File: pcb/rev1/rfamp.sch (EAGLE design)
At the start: 17 parts, among them IC1 TS520530, IC2 ADL5523, X1 SAW-B3721

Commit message: Minor changes.
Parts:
- MOV1: value MOV -> (none)
- renumbered R1 to MOV1
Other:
- moved on the sheet: C3, C4, C5, IC1, JP1, POWER, R3
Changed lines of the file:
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@@
 <part name="GND3" library="supply1" deviceset="GND" device=""/>
 <part name="X1" library="qyx-misc" deviceset="SAW-B3721" device=""/>
-<part name="R1" library="rcl" deviceset="R-EU_" device="R0603" value="MOV"/>
+<part name="MOV1" library="rcl" deviceset="R-EU_" device="R0603"/>
 <part name="GND4" library="supply1" deviceset="GND" device=""/>
 <part name="GND5" library="supply1" deviceset="GND" device=""/>
@@
 <instance part="RFIN" gate="G1" x="0" y="71.12"/>
 <instance part="GND1" gate="1" x="5.08" y="53.34"/>
-<instance part="GND2" gate="1" x="2.54" y="2.54"/>
+<instance part="GND2" gate="1" x="22.86" y="99.06"/>
 <instance part="RFOUT" gate="G1" x="182.88" y="71.12" rot="MR0"/>
 <instance part="GND3" gate="1" x="177.8" y="53.34"/>
 <instance part="X1" gate="G$1" x="53.34" y="66.04"/>
-<instance part="R1" gate="G$1" x="20.32" y="63.5" rot="R90"/>
+<instance part="MOV1" gate="G$1" x="20.32" y="63.5" rot="R90"/>
 <instance part="GND4" gate="1" x="48.26" y="53.34"/>
 <instance part="GND5" gate="1" x="53.34" y="53.34"/>
@@
 <instance part="GND10" gate="1" x="167.64" y="78.74"/>
 <instance part="+3V1" gate="G$1" x="167.64" y="99.06"/>
-<instance part="+3V2" gate="G$1" x="58.42" y="25.4"/>
-<instance part="IC1" gate="G$1" x="27.94" y="12.7"/>
-<instance part="C3" gate="G$1" x="43.18" y="10.16" rot="R90"/>
-<instance part="C4" gate="G$1" x="58.42" y="12.7"/>
-<instance part="C5" gate="G$1" x="2.54" y="12.7"/>
-<instance part="GND11" gate="1" x="15.24" y="2.54"/>
-<instance part="GND12" gate="1" x="50.8" y="2.54"/>
-<instance part="GND13" gate="1" x="58.42" y="2.54"/>
-<instance part="P+1" gate="1" x="2.54" y="25.4"/>
-<instance part="JP1" gate="G$1" x="-20.32" y="15.24"/>
-<instance part="GND14" gate="1" x="-10.16" y="2.54"/>
+<instance part="+3V2" gate="G$1" x="78.74" y="121.92"/>
+<instance part="IC1" gate="G$1" x="48.26" y="109.22"/>
+<instance part="C3" gate="G$1" x="63.5" y="106.68" rot="R90"/>
+<instance part="C4" gate="G$1" x="78.74" y="109.22"/>
+<instance part="C5" gate="G$1" x="22.86" y="109.22"/>
+<instance part="GND11" gate="1" x="35.56" y="99.06"/>
+<instance part="GND12" gate="1" x="71.12" y="99.06"/>
+<instance part="GND13" gate="1" x="78.74" y="99.06"/>
+<instance part="P+1" gate="1" x="22.86" y="121.92"/>
+<instance part="JP1" gate="G$1" x="0" y="111.76"/>
+<instance part="GND14" gate="1" x="10.16" y="99.06"/>
 <instance part="IC2" gate="G$1" x="127" y="68.58"/>
 <instance part="GND15" gate="1" x="144.78" y="53.34"/>
-<instance part="R3" gate="G$1" x="71.12" y="17.78"/>
-<instance part="POWER" gate="G$1" x="81.28" y="12.7"/>
-<instance part="GND16" gate="1" x="81.28" y="2.54"/>
+<instance part="R3" gate="G$1" x="91.44" y="114.3"/>
+<instance part="POWER" gate="G$1" x="101.6" y="109.22"/>
+<instance part="GND16" gate="1" x="101.6" y="99.06"/>
 </instances>
 <busses>
@@
 <segment>
 <pinref part="GND8" gate="1" pin="GND"/>
-<pinref part="R1" gate="G$1" pin="1"/>
+<pinref part="MOV1" gate="G$1" pin="1"/>
 <wire x1="20.32" y1="55.88" x2="20.32" y2="58.42" width="0.1524" layer="91"/>
 </segment>
@@
 <pinref part="C5" gate="G$1" pin="2"/>
 <pinref part="GND2" gate="1" pin="GND"/>
-<wire x1="2.54" y1="7.62" x2="2.54" y2="5.08" width="0.1524" layer="91"/>
+<wire x1="22.86" y1="104.14" x2="22.86" y2="101.6" width="0.1524" layer="91"/>
 </segment>
 <segment>
 <pinref part="IC1" gate="G$1" pin="GND"/>
 <pinref part="GND11" gate="1" pin="GND"/>
-<wire x1="17.78" y1="7.62" x2="15.24" y2="7.62" width="0.1524" layer="91"/>
-<wire x1="15.24" y1="7.62" x2="15.24" y2="5.08" width="0.1524" layer="91"/>
+<wire x1="38.1" y1="104.14" x2="35.56" y2="104.14" width="0.1524" layer="91"/>
+<wire x1="35.56" y1="104.14" x2="35.56" y2="101.6" width="0.1524" layer="91"/>
 </segment>
 <segment>
 <pinref part="C4" gate="G$1" pin="2"/>
 <pinref part="GND13" gate="1" pin="GND"/>
-<wire x1="58.42" y1="7.62" x2="58.42" y2="5.08" width="0.1524" layer="91"/>
+<wire x1="78.74" y1="104.14" x2="78.74" y2="101.6" width="0.1524" layer="91"/>
 </segment>
 <segment>
 <pinref part="C3" gate="G$1" pin="2"/>
 <pinref part="GND12" gate="1" pin="GND"/>
-<wire x1="48.26" y1="10.16" x2="50.8" y2="10.16" width="0.1524" layer="91"/>
-<wire x1="50.8" y1="10.16" x2="50.8" y2="5.08" width="0.1524" layer="91"/>
+<wire x1="68.58" y1="106.68" x2="71.12" y2="106.68" width="0.1524" layer="91"/>
+<wire x1="71.12" y1="106.68" x2="71.12" y2="101.6" width="0.1524" layer="91"/>
 </segment>
 <segment>
 <pinref part="JP1" gate="G$1" pin="1"/>
 <pinref part="GND14" gate="1" pin="GND"/>
-<wire x1="-12.7" y1="15.24" x2="-10.16" y2="15.24" width="0.1524" layer="91"/>
-<wire x1="-10.16" y1="15.24" x2="-10.16" y2="5.08" width="0.1524" layer="91"/>
+<wire x1="7.62" y1="111.76" x2="10.16" y2="111.76" width="0.1524" layer="91"/>
+<wire x1="10.16" y1="111.76" x2="10.16" y2="101.6" width="0.1524" layer="91"/>
 </segment>
 <segment>
@@
 <pinref part="POWER" gate="G$1" pin="C"/>
 <pinref part="GND16" gate="1" pin="GND"/>
-<wire x1="81.28" y1="7.62" x2="81.28" y2="5.08" width="0.1524" layer="91"/>
+<wire x1="101.6" y1="104.14" x2="101.6" y2="101.6" width="0.1524" layer="91"/>
 </segment>
 </net>
@@
 <segment>
 <pinref part="RFIN" gate="G1" pin="1"/>
-<pinref part="R1" gate="G$1" pin="2"/>
+<pinref part="MOV1" gate="G$1" pin="2"/>
 <wire x1="2.54" y1="71.12" x2="20.32" y2="71.12" width="0.1524" layer="91"/>
 <wire x1="20.32" y1="71.12" x2="20.32" y2="68.58" width="0.1524" layer="91"/>
@@
 <pinref part="IC1" gate="G$1" pin="VOUT"/>
 <pinref part="C4" gate="G$1" pin="1"/>
-<wire x1="38.1" y1="17.78" x2="58.42" y2="17.78" width="0.1524" layer="91"/>
-<wire x1="58.42" y1="17.78" x2="58.42" y2="15.24" width="0.1524" layer="91"/>
+<wire x1="58.42" y1="114.3" x2="78.74" y2="114.3" width="0.1524" layer="91"/>
+<wire x1="78.74" y1="114.3" x2="78.74" y2="111.76" width="0.1524" layer="91"/>
 <pinref part="+3V2" gate="G$1" pin="+3V3"/>
-<wire x1="58.42" y1="17.78" x2="58.42" y2="22.86" width="0.1524" layer="91"/>
-<junction x="58.42" y="17.78"/>
+<wire x1="78.74" y1="114.3" x2="78.74" y2="119.38" width="0.1524" layer="91"/>
+<junction x="78.74" y="114.3"/>
 <pinref part="R3" gate="G$1" pin="1"/>
-<wire x1="58.42" y1="17.78" x2="66.04" y2="17.78" width="0.1524" layer="91"/>
+<wire x1="78.74" y1="114.3" x2="86.36" y2="114.3" width="0.1524" layer="91"/>
 </segment>
 </net>
@@
 <pinref part="C5" gate="G$1" pin="1"/>
 <pinref part="P+1" gate="1" pin="+5V"/>
-<wire x1="2.54" y1="15.24" x2="2.54" y2="17.78" width="0.1524" layer="91"/>
+<wire x1="22.86" y1="111.76" x2="22.86" y2="114.3" width="0.1524" layer="91"/>
 <pinref part="IC1" gate="G$1" pin="VIN"/>
-<wire x1="2.54" y1="17.78" x2="2.54" y2="22.86" width="0.1524" layer="91"/>
-<wire x1="17.78" y1="17.78" x2="15.24" y2="17.78" width="0.1524" layer="91"/>
-<junction x="2.54" y="17.78"/>
+<wire x1="22.86" y1="114.3" x2="22.86" y2="119.38" width="0.1524" layer="91"/>
+<wire x1="38.1" y1="114.3" x2="35.56" y2="114.3" width="0.1524" layer="91"/>
+<junction x="22.86" y="114.3"/>
 <pinref part="IC1" gate="G$1" pin="CE"/>
-<wire x1="15.24" y1="17.78" x2="2.54" y2="17.78" width="0.1524" layer="91"/>
-<wire x1="17.78" y1="12.7" x2="15.24" y2="12.7" width="0.1524" layer="91"/>
-<wire x1="15.24" y1="12.7" x2="15.24" y2="17.78" width="0.1524" layer="91"/>
-<junction x="15.24" y="17.78"/>
+<wire x1="35.56" y1="114.3" x2="22.86" y2="114.3" width="0.1524" layer="91"/>
+<wire x1="38.1" y1="109.22" x2="35.56" y2="109.22" width="0.1524" layer="91"/>
+<wire x1="35.56" y1="109.22" x2="35.56" y2="114.3" width="0.1524" layer="91"/>
+<junction x="35.56" y="114.3"/>
 <pinref part="JP1" gate="G$1" pin="2"/>
-<wire x1="-12.7" y1="17.78" x2="2.54" y2="17.78" width="0.1524" layer="91"/>
+<wire x1="7.62" y1="114.3" x2="22.86" y2="114.3" width="0.1524" layer="91"/>
 </segment>
 </net>
@@
 <pinref part="C3" gate="G$1" pin="1"/>
 <pinref part="IC1" gate="G$1" pin="CB"/>
-<wire x1="40.64" y1="10.16" x2="38.1" y2="10.16" width="0.1524" layer="91"/>
+<wire x1="60.96" y1="106.68" x2="58.42" y2="106.68" width="0.1524" layer="91"/>
 </segment>
 </net>
@@
 <pinref part="R3" gate="G$1" pin="2"/>
 <pinref part="POWER" gate="G$1" pin="A"/>
-<wire x1="76.2" y1="17.78" x2="81.28" y2="17.78" width="0.1524" layer="91"/>
-<wire x1="81.28" y1="17.78" x2="81.28" y2="15.24" width="0.1524" layer="91"/>
-</segment>
-</net>
+<wire x1="96.52" y1="114.3" x2="101.6" y2="114.3" width="0.1524" layer="91"/>
+<wire x1="101.6" y1="114.3" x2="101.6" y2="111.76" width="0.1524" layer="91"/>
+</segment>
+</net>

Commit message: Replace SMA edge connectors.
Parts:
- removed RFIN, RFOUT: SMA-142-0711-821/826, con-coax:SMA-142-0711-821/826
- added J$1, J$2: SMA_EDGE, SparkFun:SMA_EDGE
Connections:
- net GND: now also J$1.GND@0, J$1.GND@1, J$1.GND@2, J$1.GND@3, J$2.GND@0, J$2.GND@1, J$2.GND@2, J$2.GND@3; no longer RFIN.2, RFOUT.2
- net N$1: now also J$1.SIGNAL; no longer RFIN.1
- net N$6: now also J$2.SIGNAL; no longer RFOUT.1

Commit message: Insert dc blocking capacitors.
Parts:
- added C6, C7, C8: 100pF, rcl:C-EUC0603
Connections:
- new net N$10: C7.1, X1.OUT
- new net N$11: C8.2, J$2.SIGNAL
- new net N$9: C6.2, X1.IN
- net N$1: now also C6.1; no longer X1.IN
- net N$2: now also C7.2; no longer X1.OUT
- net N$6: now also C8.1; no longer J$2.SIGNAL
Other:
- moved on the sheet: C1, L1, MOV1
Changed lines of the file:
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@@
 <part name="J$1" library="SparkFun" deviceset="SMA_EDGE" device=""/>
 <part name="J$2" library="SparkFun" deviceset="SMA_EDGE" device=""/>
+<part name="C6" library="rcl" deviceset="C-EU" device="C0603" value="100pF"/>
+<part name="C7" library="rcl" deviceset="C-EU" device="C0603" value="100pF"/>
+<part name="C8" library="rcl" deviceset="C-EU" device="C0603" value="100pF"/>
 </parts>
 <sheets>
@@
 <instance part="GND3" gate="1" x="172.72" y="53.34"/>
 <instance part="X1" gate="G$1" x="53.34" y="66.04"/>
-<instance part="MOV1" gate="G$1" x="20.32" y="63.5" rot="R90"/>
+<instance part="MOV1" gate="G$1" x="10.16" y="63.5" rot="R90"/>
 <instance part="GND4" gate="1" x="48.26" y="53.34"/>
 <instance part="GND5" gate="1" x="53.34" y="53.34"/>
 <instance part="GND6" gate="1" x="33.02" y="53.34"/>
 <instance part="GND7" gate="1" x="68.58" y="53.34"/>
-<instance part="GND8" gate="1" x="20.32" y="53.34"/>
-<instance part="C1" gate="G$1" x="81.28" y="63.5"/>
-<instance part="L1" gate="G$1" x="96.52" y="71.12" rot="R90"/>
-<instance part="GND9" gate="1" x="81.28" y="53.34"/>
+<instance part="GND8" gate="1" x="10.16" y="53.34"/>
+<instance part="C1" gate="G$1" x="88.9" y="63.5"/>
+<instance part="L1" gate="G$1" x="99.06" y="71.12" rot="R90"/>
+<instance part="GND9" gate="1" x="88.9" y="53.34"/>
 <instance part="R2" gate="G$1" x="127" y="91.44"/>
 <instance part="L2" gate="G$1" x="154.94" y="91.44" rot="R90"/>
@@
 <instance part="J$1" gate="1" x="-2.54" y="71.12"/>
 <instance part="J$2" gate="1" x="167.64" y="71.12" rot="MR0"/>
+<instance part="C6" gate="G$1" x="20.32" y="71.12" rot="R90"/>
+<instance part="C7" gate="G$1" x="76.2" y="71.12" rot="R90"/>
+<instance part="C8" gate="G$1" x="152.4" y="71.12" rot="R90"/>
 </instances>
 <busses>
@@
 <pinref part="GND8" gate="1" pin="GND"/>
 <pinref part="MOV1" gate="G$1" pin="1"/>
-<wire x1="20.32" y1="55.88" x2="20.32" y2="58.42" width="0.1524" layer="91"/>
+<wire x1="10.16" y1="55.88" x2="10.16" y2="58.42" width="0.1524" layer="91"/>
 </segment>
 <segment>
 <pinref part="C1" gate="G$1" pin="2"/>
 <pinref part="GND9" gate="1" pin="GND"/>
-<wire x1="81.28" y1="58.42" x2="81.28" y2="55.88" width="0.1524" layer="91"/>
+<wire x1="88.9" y1="58.42" x2="88.9" y2="55.88" width="0.1524" layer="91"/>
 </segment>
 <segment>
@@
 </segment>
 </net>
-<net name="N$1" class="1">
+<net name="N$1" class="0">
 <segment>
 <pinref part="MOV1" gate="G$1" pin="2"/>
-<wire x1="2.54" y1="71.12" x2="20.32" y2="71.12" width="0.1524" layer="91"/>
-<wire x1="20.32" y1="71.12" x2="20.32" y2="68.58" width="0.1524" layer="91"/>
-<pinref part="X1" gate="G$1" pin="IN"/>
-<wire x1="20.32" y1="71.12" x2="35.56" y2="71.12" width="0.1524" layer="91"/>
-<junction x="20.32" y="71.12"/>
+<wire x1="2.54" y1="71.12" x2="10.16" y2="71.12" width="0.1524" layer="91"/>
+<wire x1="10.16" y1="71.12" x2="10.16" y2="68.58" width="0.1524" layer="91"/>
 <pinref part="J$1" gate="1" pin="SIGNAL"/>
-</segment>
-</net>
-<net name="N$2" class="1">
-<segment>
-<pinref part="X1" gate="G$1" pin="OUT"/>
+<pinref part="C6" gate="G$1" pin="1"/>
+<wire x1="10.16" y1="71.12" x2="17.78" y2="71.12" width="0.1524" layer="91"/>
+<junction x="10.16" y="71.12"/>
+</segment>
+</net>
+<net name="N$2" class="0">
+<segment>
 <pinref part="C1" gate="G$1" pin="1"/>
-<wire x1="66.04" y1="71.12" x2="81.28" y2="71.12" width="0.1524" layer="91"/>
-<wire x1="81.28" y1="71.12" x2="81.28" y2="66.04" width="0.1524" layer="91"/>
+<wire x1="88.9" y1="71.12" x2="88.9" y2="66.04" width="0.1524" layer="91"/>
 <pinref part="L1" gate="G$1" pin="1"/>
+<wire x1="88.9" y1="71.12" x2="91.44" y2="71.12" width="0.1524" layer="91"/>
+<pinref part="C7" gate="G$1" pin="2"/>
 <wire x1="81.28" y1="71.12" x2="88.9" y2="71.12" width="0.1524" layer="91"/>
-<junction x="81.28" y="71.12"/>
+<junction x="88.9" y="71.12"/>
 </segment>
 </net>
@@
 </segment>
 </net>
-<net name="N$5" class="1">
+<net name="N$5" class="0">
 <segment>
 <pinref part="L1" gate="G$1" pin="2"/>
-<wire x1="104.14" y1="71.12" x2="111.76" y2="71.12" width="0.1524" layer="91"/>
+<wire x1="106.68" y1="71.12" x2="111.76" y2="71.12" width="0.1524" layer="91"/>
 <pinref part="IC2" gate="G$1" pin="RFIN"/>
-</segment>
-</net>
-<net name="N$6" class="1">
-<segment>
-<wire x1="162.56" y1="71.12" x2="142.24" y2="71.12" width="0.1524" layer="91"/>
-<pinref part="IC2" gate="G$1" pin="RFOUT"/>
-<pinref part="J$2" gate="1" pin="SIGNAL"/>
 </segment>
 </net>
@@
 </segment>
 </net>
+<net name="N$9" class="0">
+<segment>
+<pinref part="C6" gate="G$1" pin="2"/>
+<pinref part="X1" gate="G$1" pin="IN"/>
+<wire x1="25.4" y1="71.12" x2="35.56" y2="71.12" width="0.1524" layer="91"/>
+</segment>
+</net>
+<net name="N$10" class="0">
+<segment>
+<pinref part="X1" gate="G$1" pin="OUT"/>
+<pinref part="C7" gate="G$1" pin="1"/>
+<wire x1="66.04" y1="71.12" x2="73.66" y2="71.12" width="0.1524" layer="91"/>
+</segment>
+</net>
+<net name="N$6" class="0">
+<segment>
+<pinref part="IC2" gate="G$1" pin="RFOUT"/>
+<pinref part="C8" gate="G$1" pin="1"/>
+<wire x1="142.24" y1="71.12" x2="149.86" y2="71.12" width="0.1524" layer="91"/>
+</segment>
+</net>
+<net name="N$11" class="0">
+<segment>
+<pinref part="C8" gate="G$1" pin="2"/>
+<pinref part="J$2" gate="1" pin="SIGNAL"/>
+<wire x1="157.48" y1="71.12" x2="162.56" y2="71.12" width="0.1524" layer="91"/>
+</segment>
+</net>

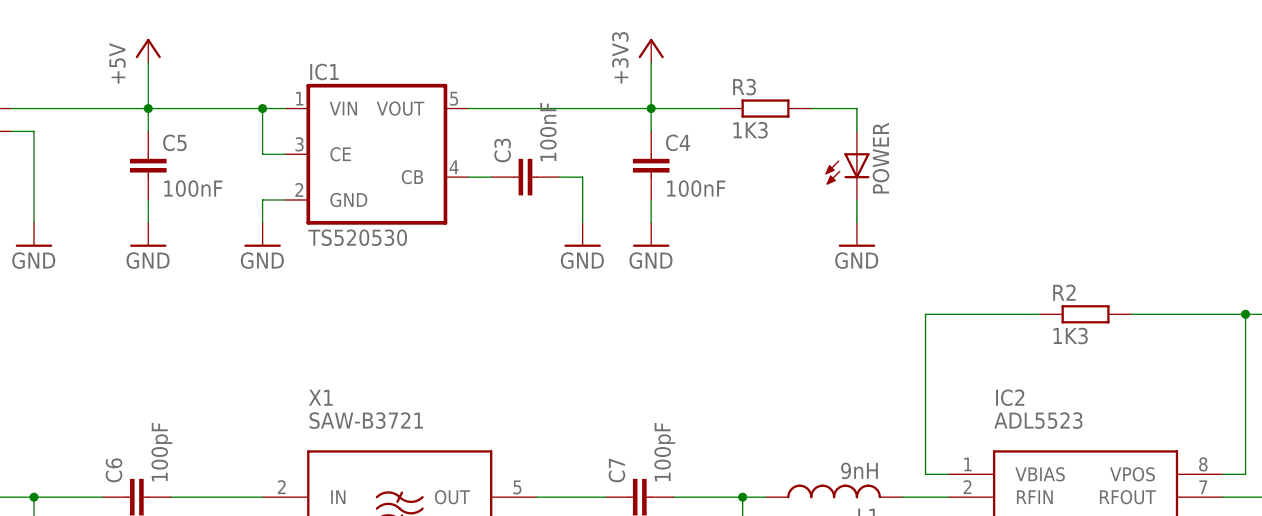
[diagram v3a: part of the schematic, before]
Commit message: Modified component values to match working prototype.
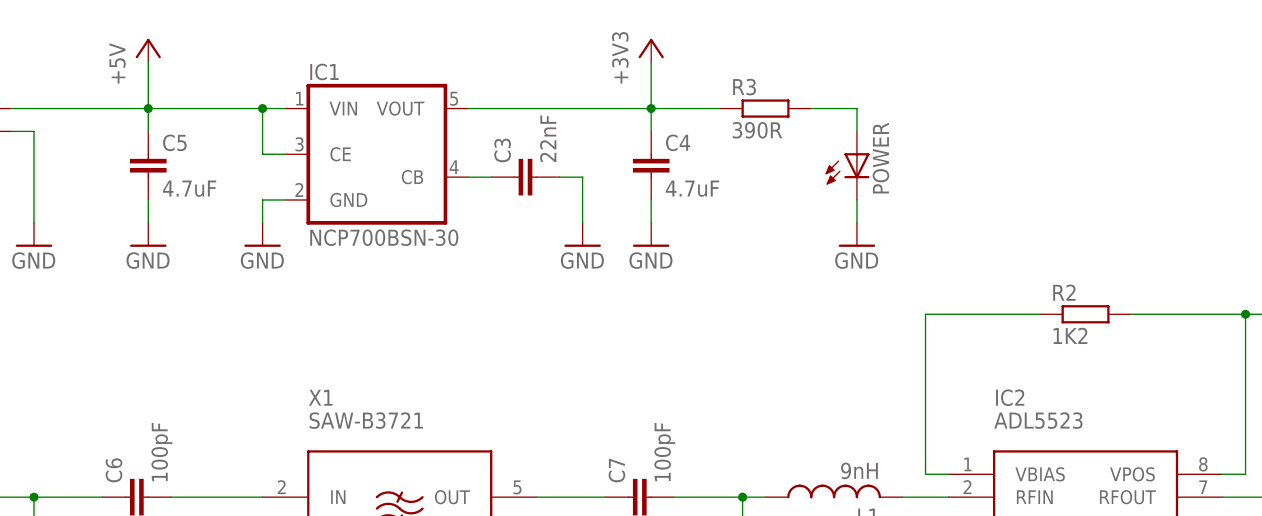
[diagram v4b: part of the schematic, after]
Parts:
- C3: value 100nF -> 22nF
- C4, C5: value 100nF -> 4.7uF
- IC1: value TS520530 -> NCP700BSN-30
- R2: value 1K3 -> 1K2
- R3: value 1K3 -> 390R
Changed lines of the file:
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@@
 <part name="L1" library="rcl" deviceset="L-US" device="L2012C" value="9nH"/>
 <part name="GND9" library="supply1" deviceset="GND" device=""/>
-<part name="R2" library="rcl" deviceset="R-EU_" device="R0603" value="1K3"/>
+<part name="R2" library="rcl" deviceset="R-EU_" device="R0603" value="1K2"/>
 <part name="L2" library="rcl" deviceset="L-US" device="L2012C" value="12nH"/>
 <part name="C2" library="rcl" deviceset="C-EU" device="C0603" value="100nF"/>
@@
 <part name="+3V1" library="supply1" deviceset="+3V3" device=""/>
 <part name="+3V2" library="supply1" deviceset="+3V3" device=""/>
-<part name="IC1" library="v-reg" deviceset="TS5205" device="" technology="30"/>
-<part name="C3" library="rcl" deviceset="C-EU" device="C0603" value="100nF"/>
-<part name="C4" library="rcl" deviceset="C-EU" device="C0805" value="100nF"/>
-<part name="C5" library="rcl" deviceset="C-EU" device="C0805" value="100nF"/>
+<part name="IC1" library="v-reg" deviceset="TS5205" device="" technology="30" value="NCP700BSN-30"/>
+<part name="C3" library="rcl" deviceset="C-EU" device="C0603" value="22nF"/>
+<part name="C4" library="rcl" deviceset="C-EU" device="C0805" value="4.7uF"/>
+<part name="C5" library="rcl" deviceset="C-EU" device="C0805" value="4.7uF"/>
 <part name="GND11" library="supply1" deviceset="GND" device=""/>
 <part name="GND12" library="supply1" deviceset="GND" device=""/>
@@
 <part name="IC2" library="qyx-misc" deviceset="ADL5523" device=""/>
 <part name="GND15" library="supply1" deviceset="GND" device=""/>
-<part name="R3" library="rcl" deviceset="R-EU_" device="R0603" value="1K3"/>
+<part name="R3" library="rcl" deviceset="R-EU_" device="R0603" value="390R"/>
 <part name="POWER" library="led" deviceset="LED" device="CHIPLED_0603"/>
 <part name="GND16" library="supply1" deviceset="GND" device=""/>
